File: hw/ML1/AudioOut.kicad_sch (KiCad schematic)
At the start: 22 parts, among them T1 Transformer_1P_1S, U1 LMV324 (Actually LTV9161), U2 LTV-356T, U4 MCP4725xxx-xCH

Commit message: Re-work of ML1 board in process
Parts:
- C5, C7: footprint KiCad-Library:CAP_KEMET_530_530 -> bruce-footprints:CAP_KEMET_530_530
- RV1: footprint KiCad-Library:POT_3362P -> bruce-footprints:POT_3362P
- T1: footprint KiCad-Library:CheapAudioTransformer -> bruce-footprints:CheapAudioTransformer
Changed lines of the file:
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@@
       (effects (font (size 1.27 1.27)))
     )
-    (property "Footprint" "KiCad-Library:CAP_KEMET_530_530" (at 177.8 86.36 0)
+    (property "Footprint" "bruce-footprints:CAP_KEMET_530_530" (at 177.8 86.36 0)
       (effects (font (size 1.27 1.27)) hide)
     )
@@
       (effects (font (size 1.27 1.27)) (justify right))
     )
-    (property "Footprint" "KiCad-Library:POT_3362P" (at 232.41 104.14 0)
+    (property "Footprint" "bruce-footprints:POT_3362P" (at 232.41 104.14 0)
       (effects (font (size 1.27 1.27)) hide)
     )
@@
       (effects (font (size 1.27 1.27)) hide)
     )
-    (property "Footprint" "KiCad-Library:CheapAudioTransformer" (at 201.93 91.44 0)
+    (property "Footprint" "bruce-footprints:CheapAudioTransformer" (at 201.93 91.44 0)
       (effects (font (size 1.27 1.27)) hide)
     )
@@
       (effects (font (size 1.27 1.27)) (justify left))
     )
-    (property "Footprint" "KiCad-Library:CAP_KEMET_530_530" (at 87.63 59.69 0)
-      (effects (font (size 1.27 1.27)) hide)
-    )
+    (property "Footprint" "bruce-footprints:CAP_KEMET_530_530" (at 87.63 59.69 0)
+      (effects (font (size 1.27 1.27)) hide)
+    )

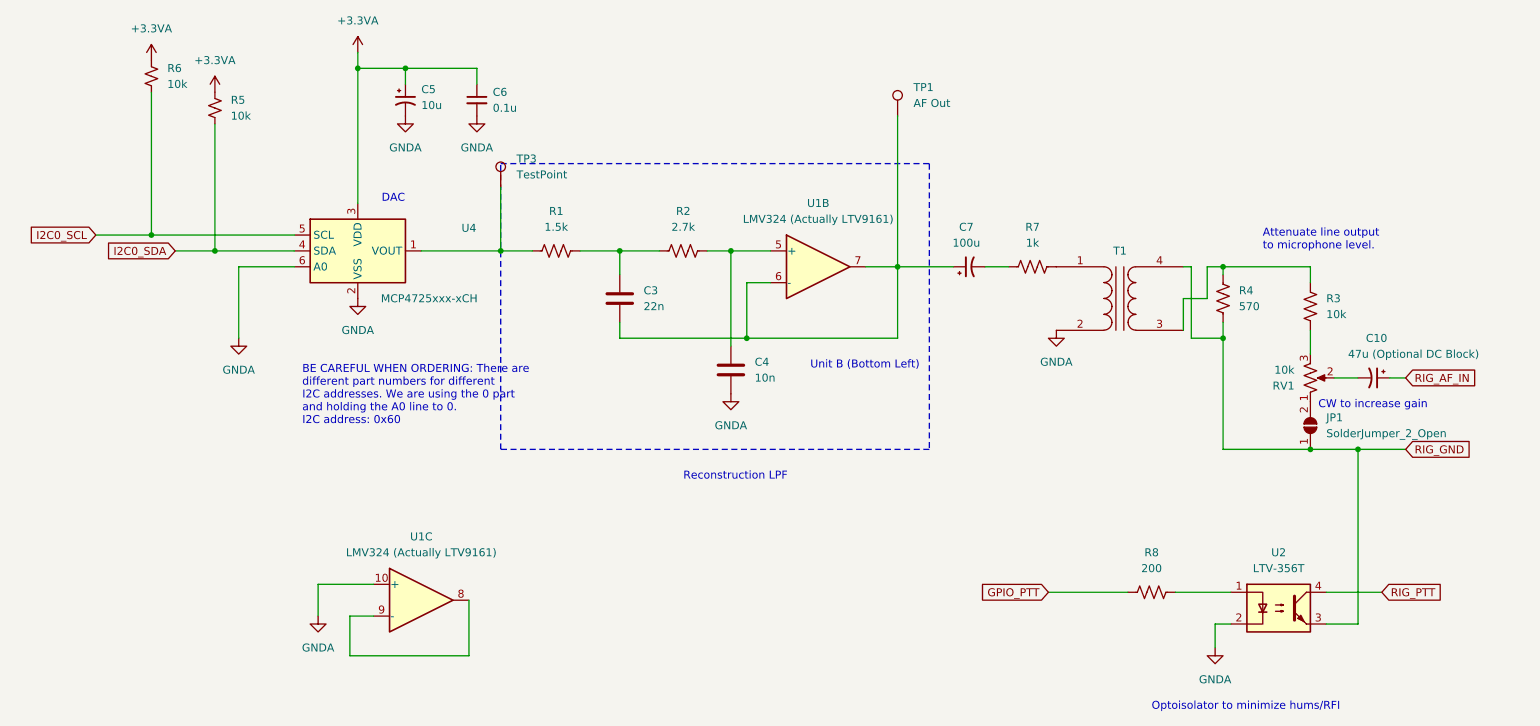
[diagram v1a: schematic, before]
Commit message: Re-work of ML1 board in process
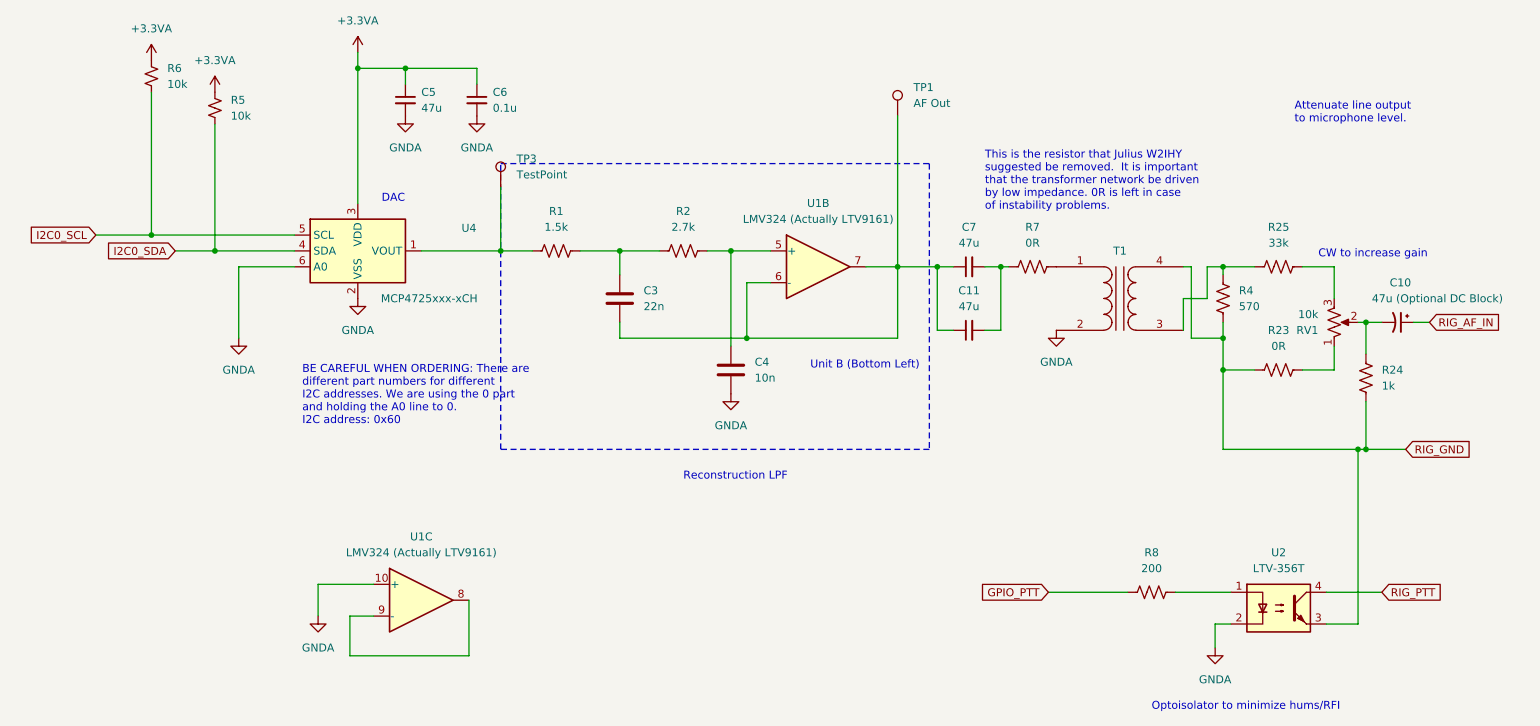
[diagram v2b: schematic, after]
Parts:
- removed C5: 10u, bruce-footprints:CAP_KEMET_530_530, symbol Device:C_Polarized_Small_US
- removed C7: 100u, bruce-footprints:CAP_KEMET_530_530, symbol Device:C_Polarized_Small_US
- removed JP1: SolderJumper_2_Open, Jumper:SolderJumper-2_P1.3mm_Open_Pad1.0x1.5mm, symbol Jumper:SolderJumper_2_Open
- added C11, C5, C7: 47u, Capacitor_SMD:C_0805_2012Metric_Pad1.18x1.45mm_HandSolder, symbol Device:C_Small
- added R23: 0R, Resistor_SMD:R_0805_2012Metric_Pad1.20x1.40mm_HandSolder, symbol Device:R_US
- added R24: 1k, Resistor_THT:R_Axial_DIN0309_L9.0mm_D3.2mm_P2.54mm_Vertical, symbol Device:R_US
- R25: renamed from R3; value 10k -> 33k
- R7: value 1k -> 0R
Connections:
- net +3.3VA: now also C5.1
- net GNDA: now also C5.2
- net RIG_GND: now also R23.1, R24.1
- net at R7.1: now also C11.2, C7.2
- net at C3.2, TP1.1, U1.6 (-)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: now also C11.1, C7.1
- net at RV1.1: now also R23.2
- net at C10.2, RV1.2: now also R24.2
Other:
- note added: "This is the resistor that Julius W2IHY suggested be removed. It is important that the transformer network be driven by low impedance. 0R is left in case of instability problems."
- moved on the sheet: C10, R25, RV1

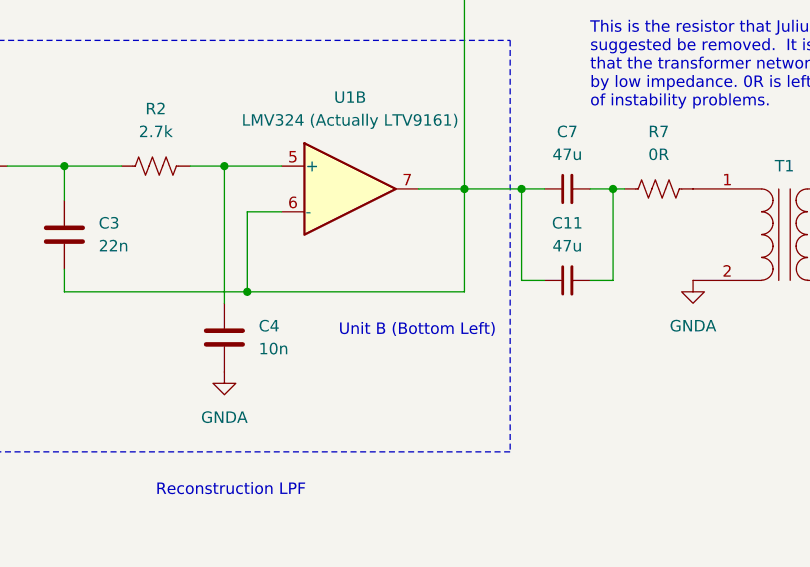
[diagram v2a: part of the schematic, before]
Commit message: First draft of board is passing DRC
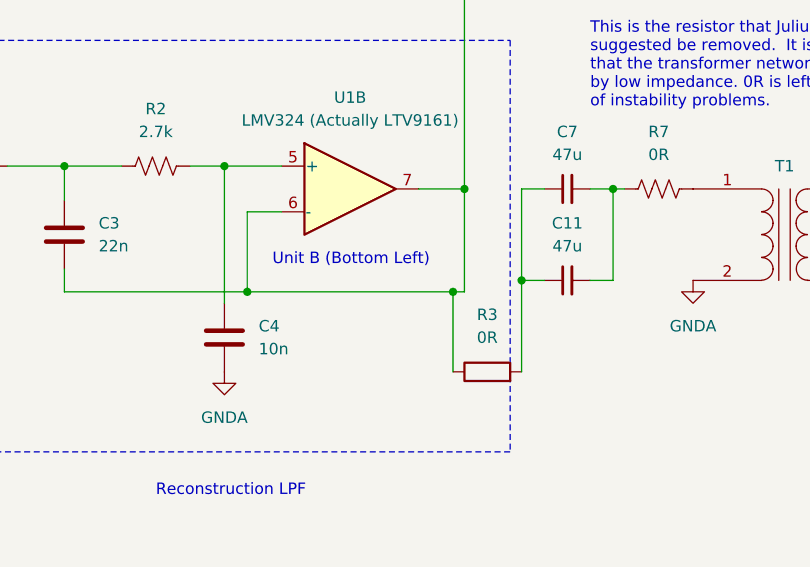
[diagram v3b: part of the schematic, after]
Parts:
- added R3: 0R, Resistor_SMD:R_1206_3216Metric_Pad1.30x1.75mm_HandSolder, symbol Device:R
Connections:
- net at C3.2, TP1.1, U1.6 (-)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: now also R3.1; no longer C11.1, C7.1
- new net: C11.1, C7.1, R3.2

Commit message: Final checks, preparing to create GRB
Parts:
- removed R7: 0R, Resistor_SMD:R_0805_2012Metric_Pad1.20x1.40mm_HandSolder, symbol Device:R_US
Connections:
- net at C11.2, C7.2: now also T1.1 (AA)
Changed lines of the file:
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@@
 	(wire
 		(pts
-			(xy 182.88 86.36) (xy 184.15 86.36)
+			(xy 182.88 86.36) (xy 191.77 86.36)
 		)
 		(stroke
@@
 			(font
 				(size 1.27 1.27)
-				(color 255 8 8 1)
+				(color 16 30 255 1)
 			)
 			(justify left bottom)
@@
 	(text "This is the resistor that Julius W2IHY \nsuggested be removed.  It is important \nthat the transformer network be driven\nby low impedance. 0R is left in case \nof instability problems."
 		(exclude_from_sim no)
-		(at 180.34 77.47 0)
+		(at 156.972 124.46 0)
 		(effects
 			(font
@@
 			)
 		)
-		(property "Description" ""
+		(property "Description" "Resistor, US symbol"
 			(at 227.33 102.87 0)
 			(effects
@@
 				(path "/5f8f636b-fd0e-498e-8696-0a023acb4c09/5945a24a-f13f-441c-8c0c-8b25494f737c"
 					(reference "R23")
-					(unit 1)
-				)
-			)
-		)
-	)
-	(symbol
-		(lib_id "Device:R_US")
-		(at 187.96 86.36 90)
-		(unit 1)
-		(exclude_from_sim no)
-		(in_bom yes)
-		(on_board yes)
-		(dnp no)
-		(fields_autoplaced yes)
-		(property "Reference" "R7"
-			(at 187.96 80.01 90)
-			(effects
-				(font
-					(size 1.27 1.27)
-				)
-			)
-		)
-		(property "Value" "0R"
-			(at 187.96 82.55 90)
-			(effects
-				(font
-					(size 1.27 1.27)
-				)
-			)
-		)
-		(property "Footprint" "Resistor_SMD:R_0805_2012Metric_Pad1.20x1.40mm_HandSolder"
-			(at 188.214 85.344 90)
-			(effects
-				(font
-					(size 1.27 1.27)
-				)
-				(hide yes)
-			)
-		)
-		(property "Datasheet" "~"
-			(at 187.96 86.36 0)
-			(effects
-				(font
-					(size 1.27 1.27)
-				)
-				(hide yes)
-			)
-		)
-		(property "Description" ""
-			(at 187.96 86.36 0)
-			(effects
-				(font
-					(size 1.27 1.27)
-				)
-				(hide yes)
-			)
-		)
-		(pin "1"
-		)
-		(pin "2"
-		)
-		(instances
-			(project "ML1"
-				(path "/5f8f636b-fd0e-498e-8696-0a023acb4c09/5945a24a-f13f-441c-8c0c-8b25494f737c"
-					(reference "R7")
 					(unit 1)
 				)
@@
 			)
 		)
-		(property "Description" ""
+		(property "Description" "Power symbol creates a global label with name \"+3.3VA\""
 			(at 57.15 58.42 0)
 			(effects
@@
 			)
 		)
-		(property "Description" ""
+		(property "Description" "Resistor, US symbol"
 			(at 218.44 91.44 0)
 			(effects
@@
 			)
 		)
-		(property "Description" ""
+		(property "Description" "Unpolarized capacitor, small symbol"
 			(at 177.8 86.36 0)
 			(effects
@@
 			)
 		)
-		(property "Description" ""
+		(property "Description" "Power symbol creates a global label with name \"GNDA\" , analog ground"
 			(at 217.17 147.32 0)
 			(effects
@@
 			)
 		)
-		(property "Description" ""
+		(property "Description" "test point"
 			(at 102.87 73.66 0)
 			(effects
@@
 			)
 		)
-		(property "Description" ""
+		(property "Description" "Power symbol creates a global label with name \"GNDA\" , analog ground"
 			(at 87.63 62.23 0)
 			(effects
@@
 			)
 		)
-		(property "Description" ""
+		(property "Description" "Power symbol creates a global label with name \"GNDA\" , analog ground"
 			(at 73.66 142.24 0)
 			(effects
@@
 			)
 		)
-		(property "Description" ""
+		(property "Description" "Unpolarized capacitor, small symbol"
 			(at 177.8 96.52 0)
 			(effects
@@
 			)
 		)
-		(property "Description" ""
+		(property "Description" "Quad Low-Voltage Rail-to-Rail Output Operational Amplifier, SOIC-14/SSOP-14"
 			(at 153.67 86.36 0)
 			(effects
@@
 			)
 		)
-		(property "Description" ""
+		(property "Description" "test point"
 			(at 166.37 62.23 0)
 			(effects
@@
 			)
 		)
-		(property "Description" ""
+		(property "Description" "DC Optocoupler, Vce 80V, CTR 50%, SO-4"
 			(at 227.33 140.97 0)
 			(effects
@@
 			)
 		)
-		(property "Description" ""
+		(property "Description" "Power symbol creates a global label with name \"+3.3VA\""
 			(at 46.99 53.34 0)
 			(effects
@@
 			)
 		)
-		(property "Description" ""
+		(property "Description" "Resistor, small US symbol"
 			(at 46.99 55.88 0)
 			(effects
@@
 			)
 		)
-		(property "Description" ""
+		(property "Description" "Unpolarized capacitor, small symbol"
 			(at 99.06 59.69 0)
 			(effects
@@
 			)
 		)
-		(property "Description" ""
+		(property "Description" "Resistor, small US symbol"
 			(at 57.15 60.96 0)
 			(effects
@@
 			)
 		)
-		(property "Description" ""
+		(property "Description" "Power symbol creates a global label with name \"GNDA\" , analog ground"
 			(at 191.77 96.52 0)
 			(effects
@@
 			)
 		)
-		(property "Description" ""
+		(property "Description" "Unpolarized capacitor"
 			(at 139.7 102.87 0)
 			(effects
@@
 			)
 		)
-		(property "Description" ""
+		(property "Description" "Resistor, US symbol"
 			(at 207.01 138.43 0)
 			(effects
@@
 			)
 		)
-		(property "Description" ""
+		(property "Description" "Unpolarized capacitor, small symbol"
 			(at 87.63 59.69 0)
 			(effects
@@
 			)
 		)
-		(property "Description" ""
+		(property "Description" "Potentiometer, US symbol"
 			(at 236.22 95.25 0)
 			(effects
@@
 			)
 		)
-		(property "Description" ""
+		(property "Description" "Resistor, US symbol"
 			(at 111.76 83.82 0)
 			(effects
@@
 			)
 		)
-		(property "Description" ""
+		(property "Description" "Resistor, US symbol"
 			(at 227.33 86.36 0)
 			(effects
@@
 			)
 		)
-		(property "Description" ""
+		(property "Description" "Resistor, US symbol"
 			(at 241.3 104.14 0)
 			(effects
@@
 			)
 		)
-		(property "Description" ""
+		(property "Description" "Resistor, US symbol"
 			(at 132.08 83.82 0)
 			(effects
@@
 			)
 		)
-		(property "Description" ""
+		(property "Description" "Power symbol creates a global label with name \"+3.3VA\""
 			(at 80.01 52.07 0)
 			(effects
@@
 			)
 		)
-		(property "Description" ""
+		(property "Description" "Power symbol creates a global label with name \"GNDA\" , analog ground"
 			(at 139.7 106.68 0)
 			(effects
@@
 			)
 		)
-		(property "Description" ""
+		(property "Description" "Quad Low-Voltage Rail-to-Rail Output Operational Amplifier, SOIC-14/SSOP-14"
 			(at 90.17 139.7 0)
 			(effects
@@
 			)
 		)
-		(property "Description" ""
+		(property "Description" "12-bit Digital-to-Analog Converter, integrated EEPROM, I2C interface, SOT-23-6"
 			(at 80.01 83.82 0)
 			(effects
@@
 			)
 		)
-		(property "Description" ""
+		(property "Description" "Transformer, single primary, single secondary"
 			(at 201.93 91.44 0)
 			(effects
@@
 			)
 		)
-		(property "Description" ""
+		(property "Description" "Power symbol creates a global label with name \"GNDA\" , analog ground"
 			(at 80.01 91.44 0)
 			(effects
@@
 			)
 		)
-		(property "Description" ""
+		(property "Description" "Polarized capacitor, small US symbol"
 			(at 246.38 95.25 0)
 			(effects
@@
 			)
 		)
-		(property "Description" ""
+		(property "Description" "Unpolarized capacitor"
 			(at 121.92 91.44 0)
 			(effects
@@
 			)
 		)
-		(property "Description" ""
+		(property "Description" "Power symbol creates a global label with name \"GNDA\" , analog ground"
 			(at 60.96 97.79 0)
 			(effects
@@
 			)
 		)
-		(property "Description" ""
+		(property "Description" "Power symbol creates a global label with name \"GNDA\" , analog ground"
 			(at 99.06 62.23 0)
 			(effects
